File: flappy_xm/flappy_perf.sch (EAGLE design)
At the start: 6 parts

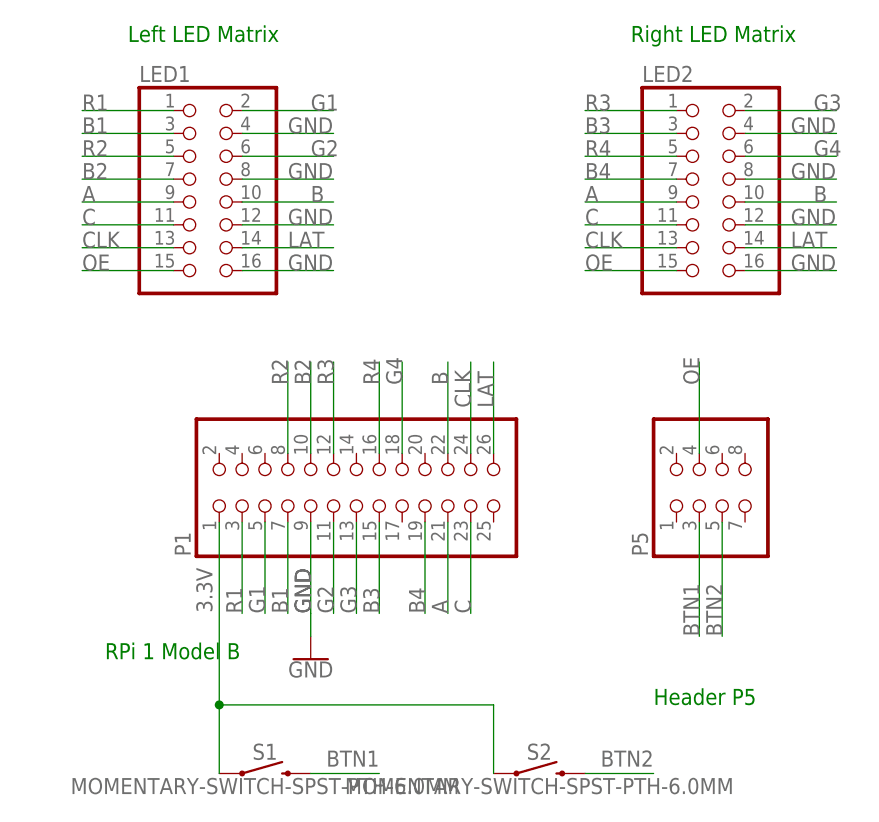
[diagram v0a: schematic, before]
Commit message: Redo wire config to be the same as in the RPI LED matrix library
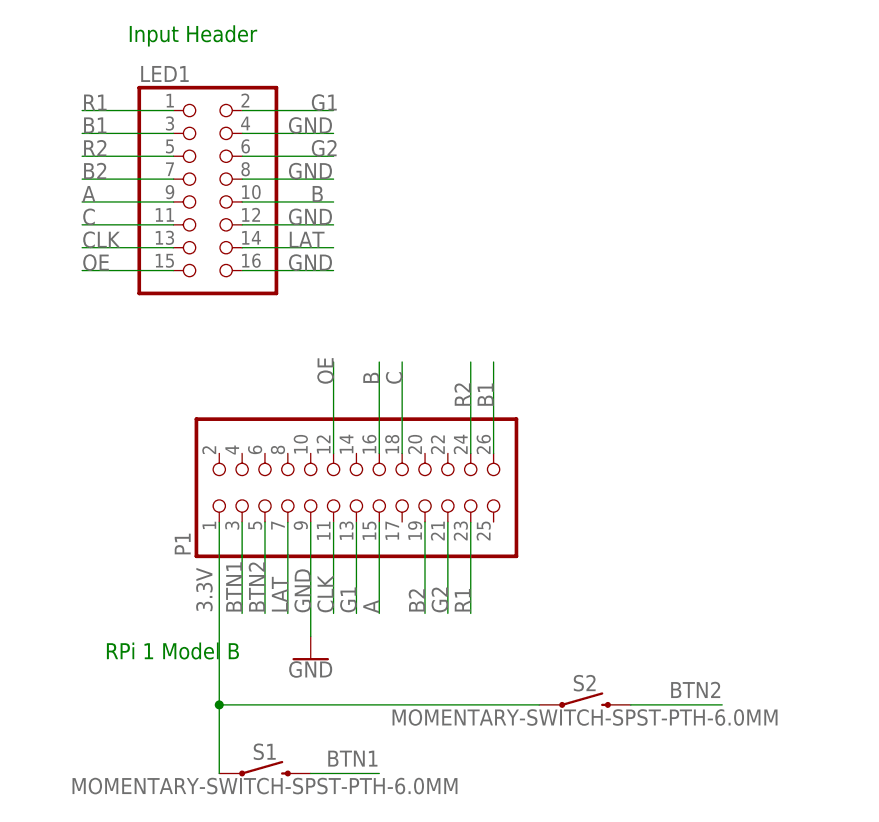
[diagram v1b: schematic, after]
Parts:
- removed LED2: (no value), pinhead:PINHD-2X8
- removed P5: (no value), pinhead:PINHD-2X4
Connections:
- removed net B3: LED2.3, P1.15
- removed net B4: LED2.7, P1.19
- removed net G3: LED2.2, P1.13
- removed net G4: LED2.6, P1.18
- removed net R3: LED2.1, P1.12
- removed net R4: LED2.5, P1.16
- net A: now also P1.15; no longer LED2.9, P1.21
- net B: now also P1.16; no longer LED2.10, P1.22
- net B1: now also P1.26; no longer P1.7
- net B2: now also P1.19; no longer P1.10
- net BTN1: now also P1.3; no longer P5.3
- net BTN2: now also P1.5; no longer P5.5
- net C: now also P1.18; no longer LED2.11, P1.23
- net CLK: now also P1.11; no longer LED2.13, P1.24
- net G1: now also P1.13; no longer P1.5
- net G2: now also P1.21; no longer P1.11
- net GND: no longer LED2.12, LED2.16, LED2.4, LED2.8
- net LAT: now also P1.7; no longer LED2.14, P1.26
- net OE: now also P1.12; no longer LED2.15, P5.4
- net R1: now also P1.23; no longer P1.3
- net R2: now also P1.24; no longer P1.8
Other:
- note added: "Input Header"
- note removed: "Header P5"
- note removed: "Left LED Matrix"
- note removed: "Right LED Matrix"
- moved on the sheet: S2
